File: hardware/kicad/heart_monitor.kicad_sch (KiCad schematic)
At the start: 28 parts, among them SW1 SW_Push, U1 TM4C123GH6PMI7, U2 MAX30102EFD+T, U3 TPS7A0318PDBVR, Y1 16MHz

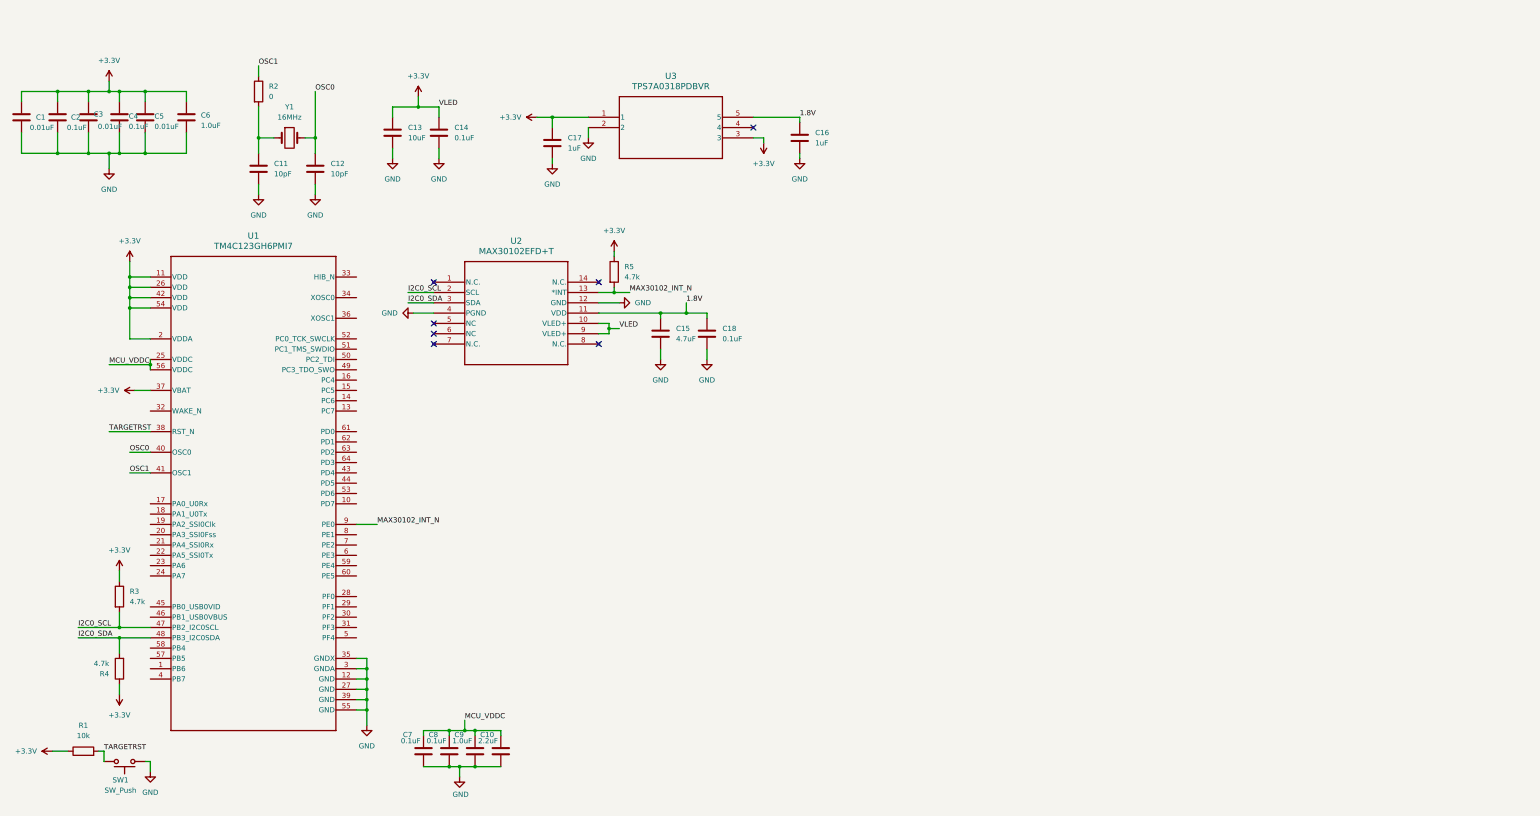
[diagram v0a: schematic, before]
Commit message: Add power, MAX30102, and SWD debug circuitry
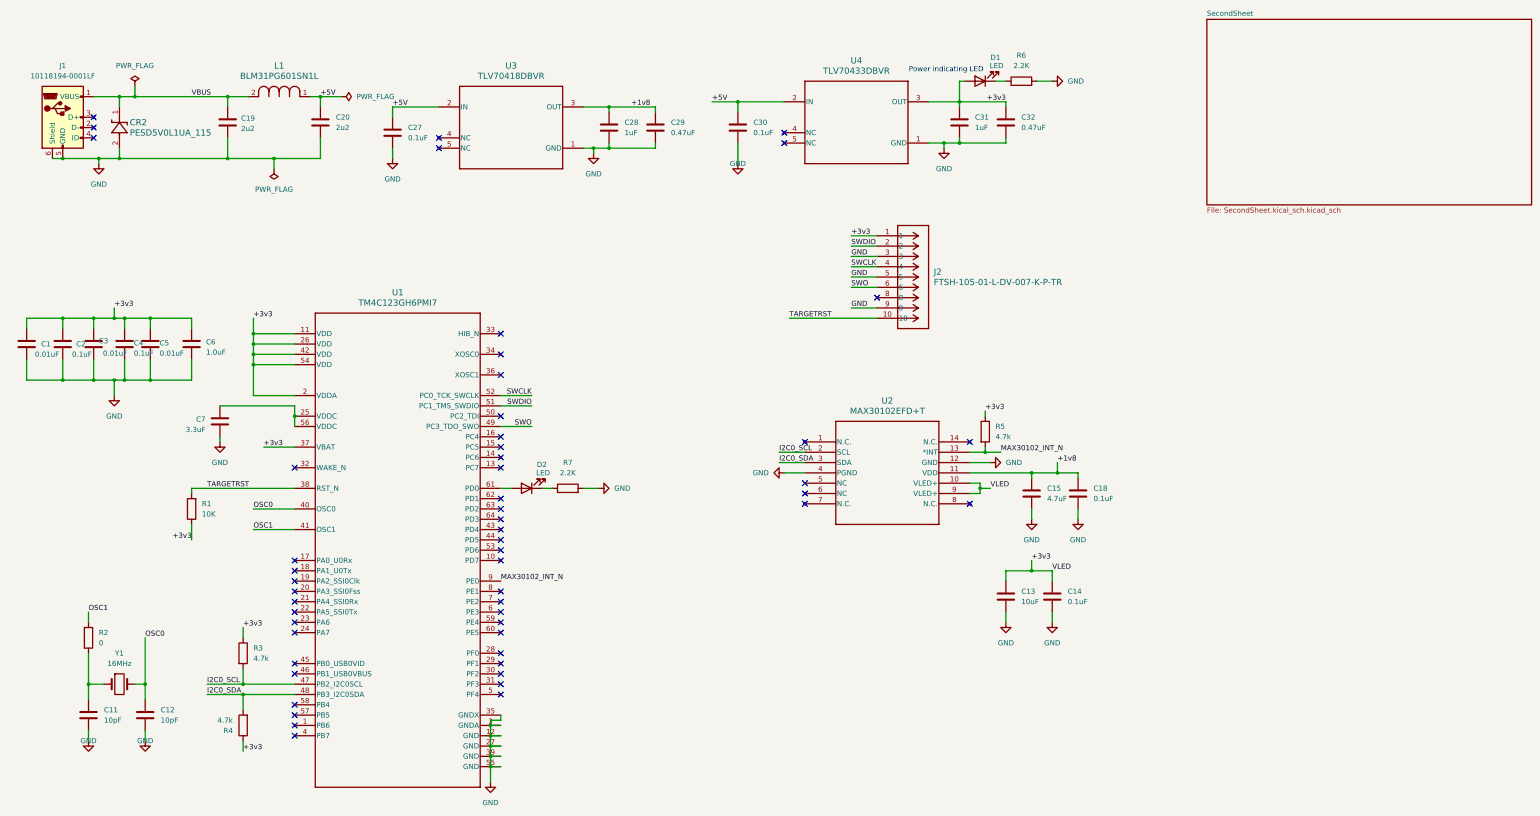
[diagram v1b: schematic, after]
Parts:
- removed C10: 2.2uF, symbol Device:C
- removed C16, C17: 1uF, symbol Device:C
- removed C8: 0.1uF, symbol Device:C
- removed C9: 1.0uF, symbol Device:C
- removed SW1: SW_Push, symbol Switch:SW_Push
- removed U3: TPS7A0318PDBVR, SOT23-5_DBV_TEX, symbol TPS7A:TPS7A0312PDBVR
- added C19, C20: 2u2, symbol Device:C
- added C27, C30: 0.1uF, symbol Device:C
- added C28, C31: 1uF, symbol Device:C
- added C29, C32: 0.47uF, symbol Device:C
- added CR2: PESD5V0L1UA_115, ZDO_SOD323_NEX, symbol 2026-08-09_18-03-51:PESD5V0L1UA_115
- added D1, D2: LED, LED_SMD:LED_0805_2012Metric, symbol Device:LED
- added J1: 10118194-0001LF, Connector_USB:USB_Micro-B_Amphenol_10118194-0001LF_Horizontal, symbol Connector:USB_B_Micro
- added J2: FTSH-105-01-L-DV-007-K-P-TR, CONN_FTSH-105-01-L-DV-007-K-P-TR_SAI, symbol 2026-08-09_19-17-37:FTSH-105-01-L-DV-007-K-P-TR
- added L1: BLM31PG601SN1L, IND_BLM31PG391SN1L_MUR, symbol 2026-08-09_18-00-03:BLM31PG601SN1L
- added R6, R7: 2.2K, symbol Device:R
- added U3: TLV70418DBVR, DBV0005A_N, symbol 2026-08-09_17-36-23:TLV70418DBVR
- added U4: TLV70433DBVR, DBV0005A_N, symbol 2026-08-09_17-34-23:TLV70433DBVR
- C7: value 0.1uF -> 3.3uF
- R1: value 10k -> 10K
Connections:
- net GND: now also C19.2, C20.2, C27.2, C28.2, C29.2, C30.2, C31.2, C32.2, CR2.2, J1.5 (GND), J1.6 (Shield), J2.3, J2.5, J2.9, R6.2, R7.2, U3.1 (GND), U4.1 (GND)
- net TARGETRST: now also J2.10
- net SWO: now reaches U1.49 (PC3_TDO_SWO)
- net SWO: now also J2.6
- net SWDIO: now reaches U1.51 (PC1_TMS_SWDIO)
- net SWDIO: now also J2.2
- net SWCLK: now reaches U1.52 (PC0_TCK_SWCLK)
- net SWCLK: now also J2.4
- net at U1.61 (PD0): now also D2.2 (A)
- net +3.3V renamed +3v3
- net +3v3: now also C31.1, C32.1, D1.2 (A), J2.1, U4.3 (OUT)
- net 1.8V renamed +1v8
- net +1v8: now also C28.1, C29.1, U3.3 (OUT)
- net MCU_VDDC: no longer names the net of C7.1, U1.25 (VDDC), U1.56 (VDDC)
- new net: D2.1 (K), R7.1
- new net: D1.1 (K), R6.1
- new net +5V: C20.1, C27.1, C30.1, L1.1, U3.2 (IN), U4.2 (IN)
- new net VBUS: C19.1, CR2.1, J1.1 (VBUS), L1.2
- no-connect marks 7 -> 54
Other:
- added sheet SecondSheet (SecondSheet.kical_sch.kicad_sch)
- note added: "Power indicating LED"
- moved on the sheet: C1, C11, C12, C13, C14, C15, C18, C2, C3, C4, C5, C6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
